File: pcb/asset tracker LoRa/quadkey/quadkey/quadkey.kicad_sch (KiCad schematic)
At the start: 0 parts

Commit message: quadkey
quadkey print klaar
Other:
- added sheet voeding (voeding.kicad_sch)
- sheet mcu ports: added none; removed RX, TX, VBAT
- company: (none) -> eurocircuits 
- title: (none) -> quadkey

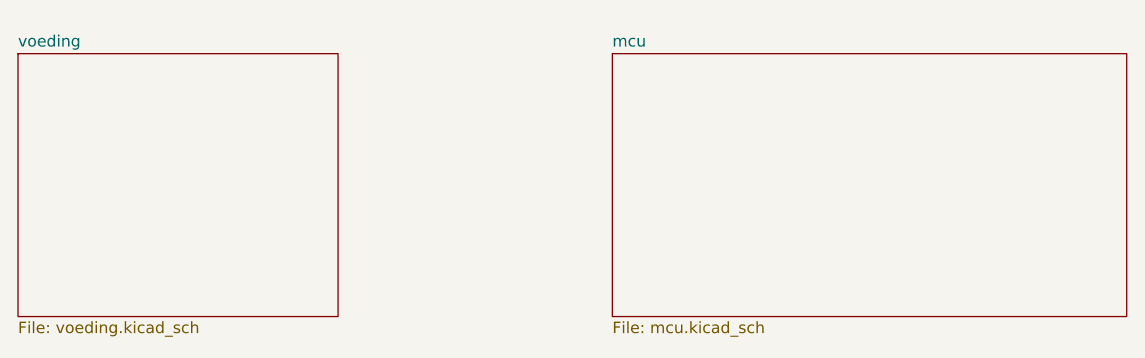
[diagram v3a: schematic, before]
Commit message: versie2
aan versie 2 begonnen met tekenen en code beginnen schrijven voor quadkey
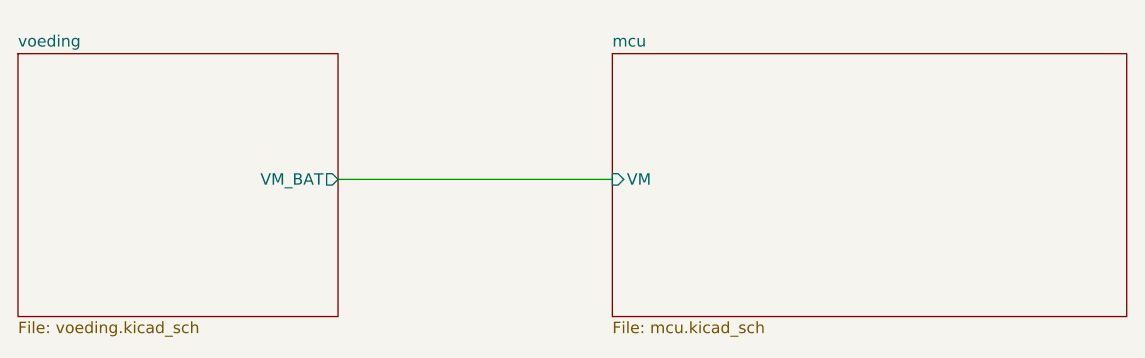
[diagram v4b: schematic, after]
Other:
- sheet mcu ports: added VM; removed none
- sheet voeding ports: added VM_BAT; removed none
